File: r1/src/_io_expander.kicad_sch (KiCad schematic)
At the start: 7 parts, among them U6 PCA9555PW

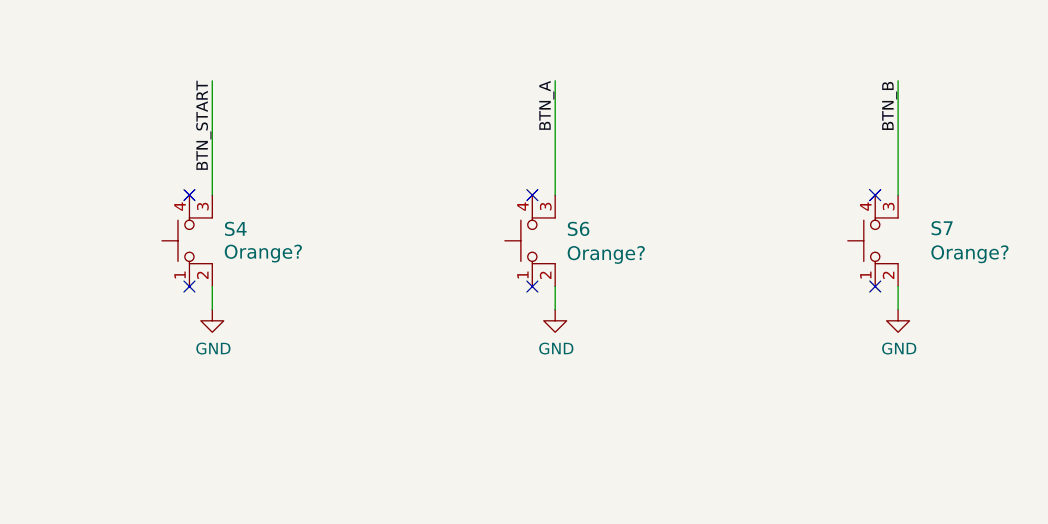
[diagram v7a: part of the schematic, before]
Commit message: ERC pass. Schematic complete.
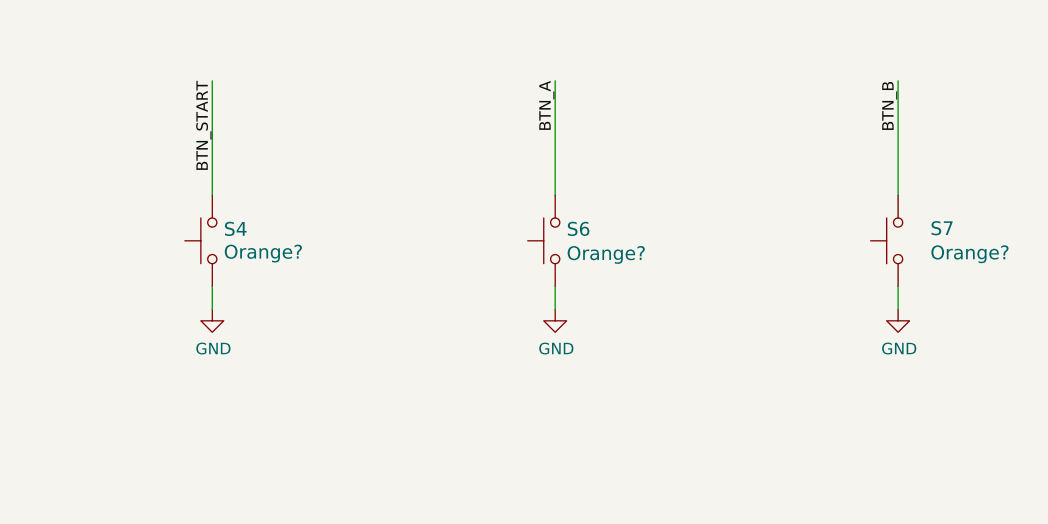
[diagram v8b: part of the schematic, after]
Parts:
- S4, S6, S7: symbol Switch:SW_MEC_5E -> Switch:SW_Push
- S5: footprint jeffmakes_footprints:SW_JS1400BFQ-arrows -> jeffmakes-footprints:SW_JS1400BFQ-arrows
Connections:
- net BTN_A: now also S6.2; no longer S6.3 (K)
- net BTN_B: now also S7.2; no longer S7.3 (K)
- net BTN_START: now also S4.2; no longer S4.3 (K)
- net GND: now also S4.1, S6.1, S7.1; no longer S4.2, S6.2, S7.2
- no-connect marks 6 -> 0
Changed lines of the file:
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@@
   (junction (at 77.47 33.02) (diameter 0) (color 0 0 0 0)
   )
-  (no_connect (at 128.27 54.61))
-  (no_connect (at 204.47 54.61))
-  (no_connect (at 204.47 44.45))
-  (no_connect (at 166.37 54.61))
-  (no_connect (at 166.37 44.45))
-  (no_connect (at 128.27 44.45))
   (wire (pts (xy 92.71 62.23) (xy 100.33 62.23))
     (stroke (width 0) (type default))
@@
       (effects (font (size 1.27 1.27)))
     )
-    (property "Footprint" "jeffmakes_footprints:SW_JS1400BFQ-arrows" (at 166.37 97.79 0)
+    (property "Footprint" "jeffmakes-footprints:SW_JS1400BFQ-arrows" (at 166.37 97.79 0)
       (effects (font (size 1.27 1.27)) (justify left bottom) hide)
     )
@@
     )
   )
-  (symbol (lib_id "Switch:SW_MEC_5E") (at 130.81 49.53 90) (unit 1)
+  (symbol (lib_id "Switch:SW_Push") (at 130.81 49.53 90) (unit 1)
     (in_bom yes) (on_board yes) (dnp no)
     (property "Reference" "S4" (at 132.08 48.26 90)
@@
       (effects (font (size 1.524 1.524)) (justify right))
     )
-    (property "Footprint" "Button_Switch_SMD:SW_SPST_PTS645" (at 123.19 49.53 0)
-      (effects (font (size 1.27 1.27)) hide)
-    )
-    (property "Datasheet" "http://www.apem.com/int/index.php?controller=attachment&id_attachment=1371" (at 123.19 49.53 0)
+    (property "Footprint" "Button_Switch_SMD:SW_SPST_PTS645" (at 125.73 49.53 0)
+      (effects (font (size 1.27 1.27)) hide)
+    )
+    (property "Datasheet" "~" (at 125.73 49.53 0)
       (effects (font (size 1.27 1.27)) hide)
     )
@@
     (pin "1")
     (pin "2")
-    (pin "3")
-    (pin "4")
     (instances
       (project "tr23-badge-r1"
@@
     )
   )
-  (symbol (lib_id "Switch:SW_MEC_5E") (at 168.91 49.53 90) (unit 1)
+  (symbol (lib_id "Switch:SW_Push") (at 168.91 49.53 90) (unit 1)
     (in_bom yes) (on_board yes) (dnp no)
     (property "Reference" "S6" (at 170.18 48.26 90)
@@
       (effects (font (size 1.524 1.524)) (justify right))
     )
-    (property "Footprint" "Button_Switch_SMD:SW_SPST_PTS645" (at 161.29 49.53 0)
-      (effects (font (size 1.27 1.27)) hide)
-    )
-    (property "Datasheet" "http://www.apem.com/int/index.php?controller=attachment&id_attachment=1371" (at 161.29 49.53 0)
+    (property "Footprint" "Button_Switch_SMD:SW_SPST_PTS645" (at 163.83 49.53 0)
+      (effects (font (size 1.27 1.27)) hide)
+    )
+    (property "Datasheet" "~" (at 163.83 49.53 0)
       (effects (font (size 1.27 1.27)) hide)
     )
@@
     (pin "1")
     (pin "2")
-    (pin "3")
-    (pin "4")
     (instances
       (project "tr23-badge-r1"
@@
     )
   )
-  (symbol (lib_id "Switch:SW_MEC_5E") (at 207.01 49.53 90) (unit 1)
+  (symbol (lib_id "Switch:SW_Push") (at 207.01 49.53 90) (unit 1)
     (in_bom yes) (on_board yes) (dnp no)
     (property "Reference" "S7" (at 210.5914 48.1838 90)
@@
       (effects (font (size 1.524 1.524)) (justify right))
     )
-    (property "Footprint" "Button_Switch_SMD:SW_SPST_PTS645" (at 199.39 49.53 0)
-      (effects (font (size 1.27 1.27)) hide)
-    )
-    (property "Datasheet" "http://www.apem.com/int/index.php?controller=attachment&id_attachment=1371" (at 199.39 49.53 0)
+    (property "Footprint" "Button_Switch_SMD:SW_SPST_PTS645" (at 201.93 49.53 0)
+      (effects (font (size 1.27 1.27)) hide)
+    )
+    (property "Datasheet" "~" (at 201.93 49.53 0)
       (effects (font (size 1.27 1.27)) hide)
     )
@@
     (pin "1")
     (pin "2")
-    (pin "3")
-    (pin "4")
-    (instances
-      (project "tr23-badge-r1"
+    (instances
+      (project "tr23-badge-r1"
